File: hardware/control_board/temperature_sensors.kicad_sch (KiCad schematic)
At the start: 24 parts, among them J5 PT100, J5 TC, U2 MAX6675, U5 MCP6N11-005, U7 MCP6001

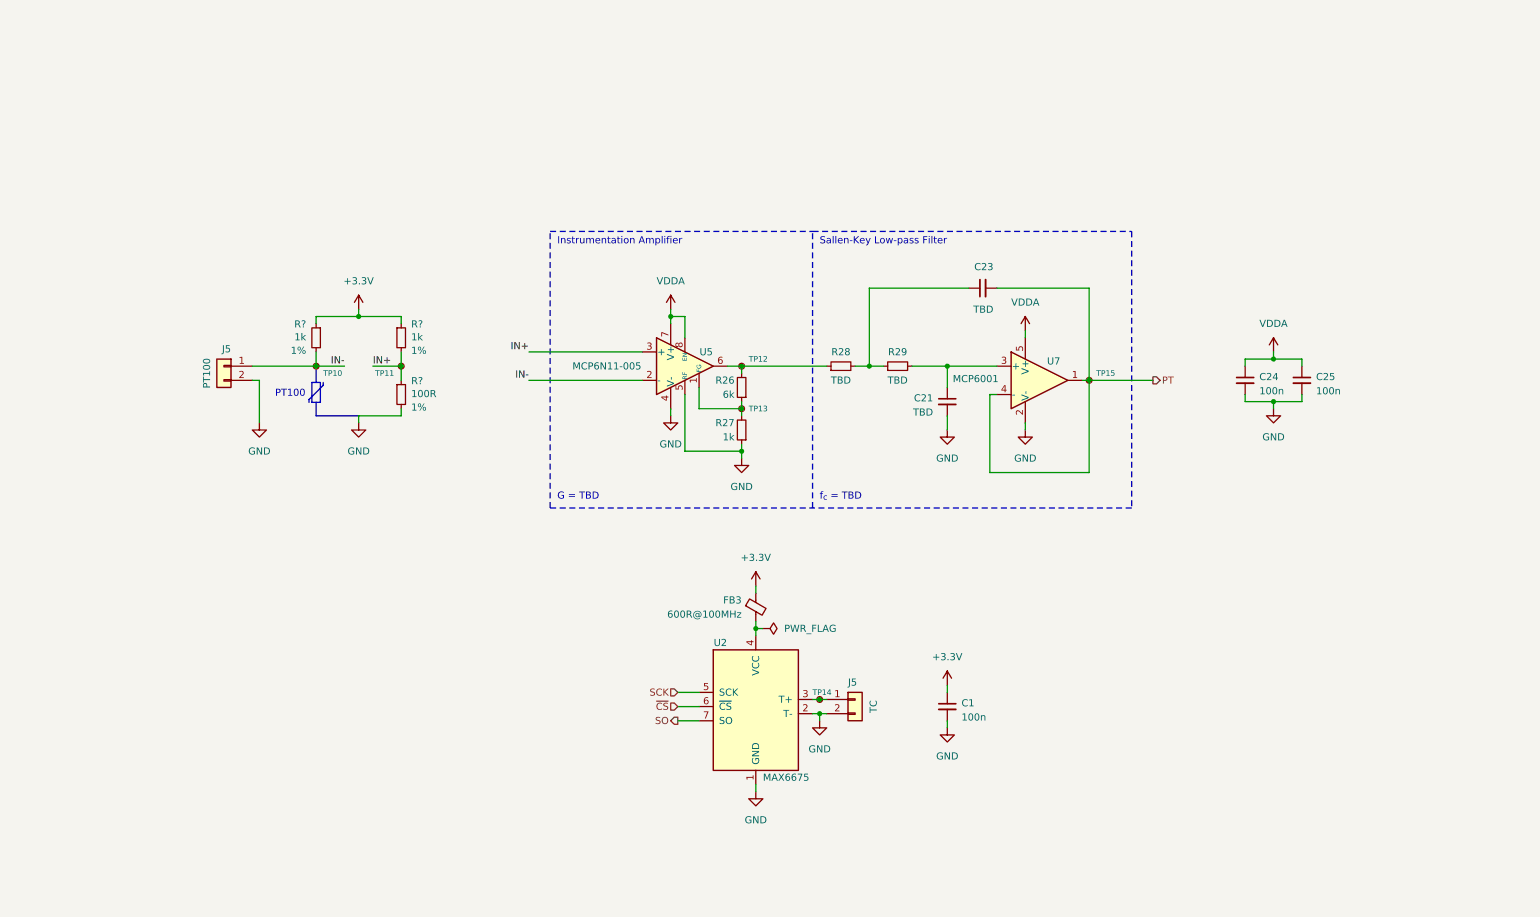
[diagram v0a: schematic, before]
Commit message: Adjust component values
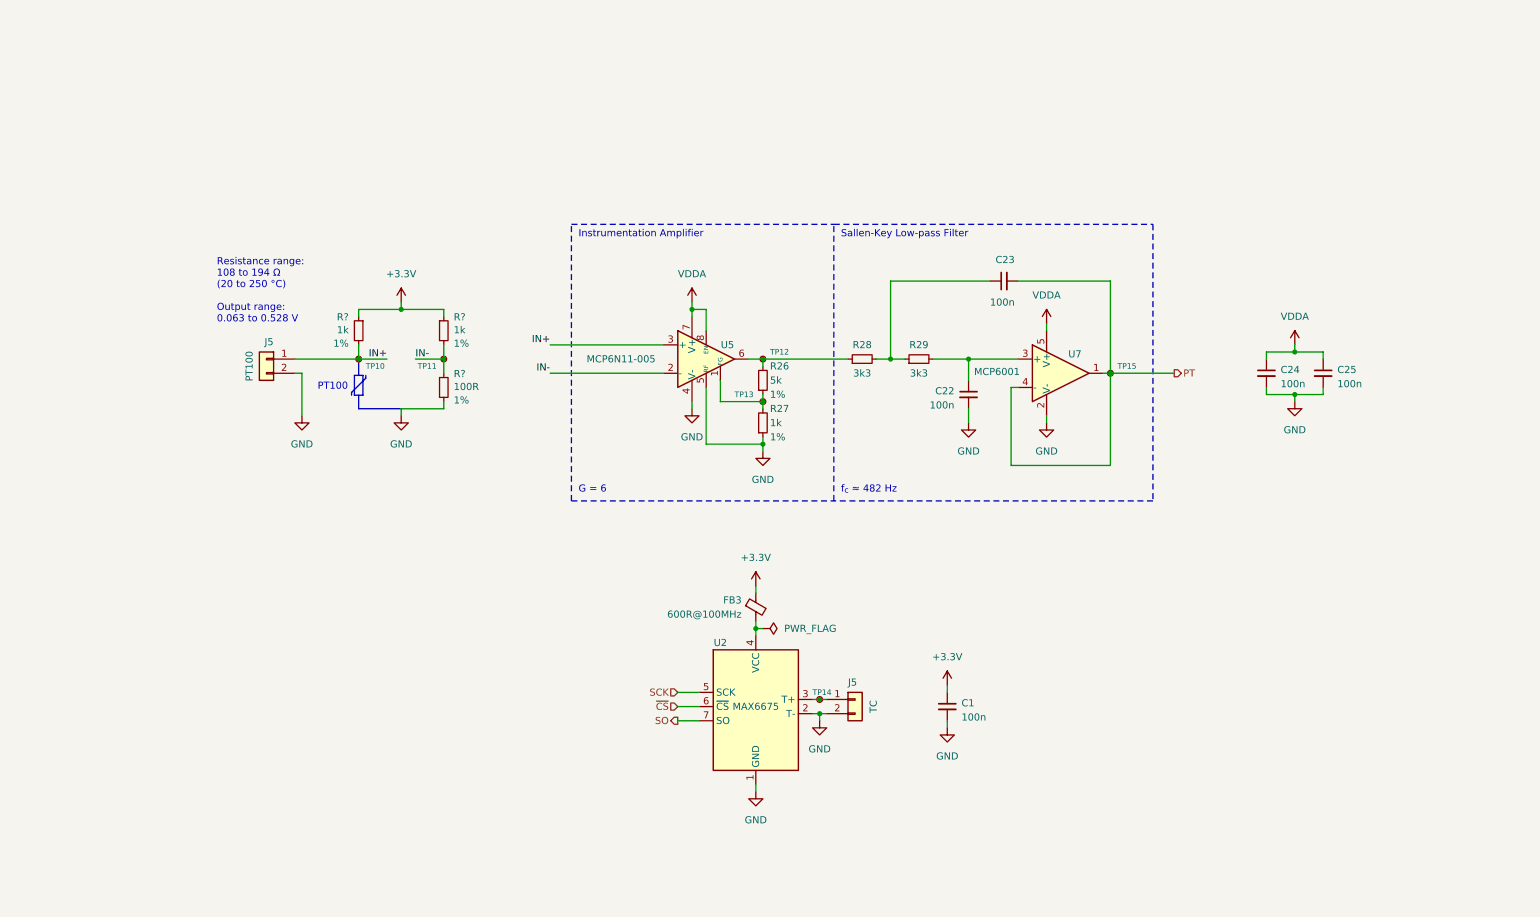
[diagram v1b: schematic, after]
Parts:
- C22: renamed from C21; value TBD -> 100n
- C23: value TBD -> 100n
- FB3: footprint (none) -> Inductor_SMD:L_0603_1608Metric
- R26: value 6k -> 5k; Tolerance (none) -> 1%
- R27: Tolerance (none) -> 1%
- R28, R29: value TBD -> 3k3
- U5: value MCP6N11-005 -> MCP6N11-005
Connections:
- net IN+: now also J5.1 (Pin_1), R?.2, TP10.1; no longer R?.1, R?.2, TP11.1
- net IN-: now also R?.1, R?.2, TP11.1; no longer J5.1 (Pin_1), R?.2, TP10.1
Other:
- note added: "G = 6"
- note added: "Resistance range: 108 to 194 Ω (20 to 250 °C) Output range: 0.063 to 0.528 V"
- note added: "f_{c} ≈ 482 Hz"
- note removed: "G = TBD"
- note removed: "f_{c} = TBD"
- moved on the sheet: C22, C23, C24, C25, J5, R26, R27, R28, R29, R?, TP10, TP11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

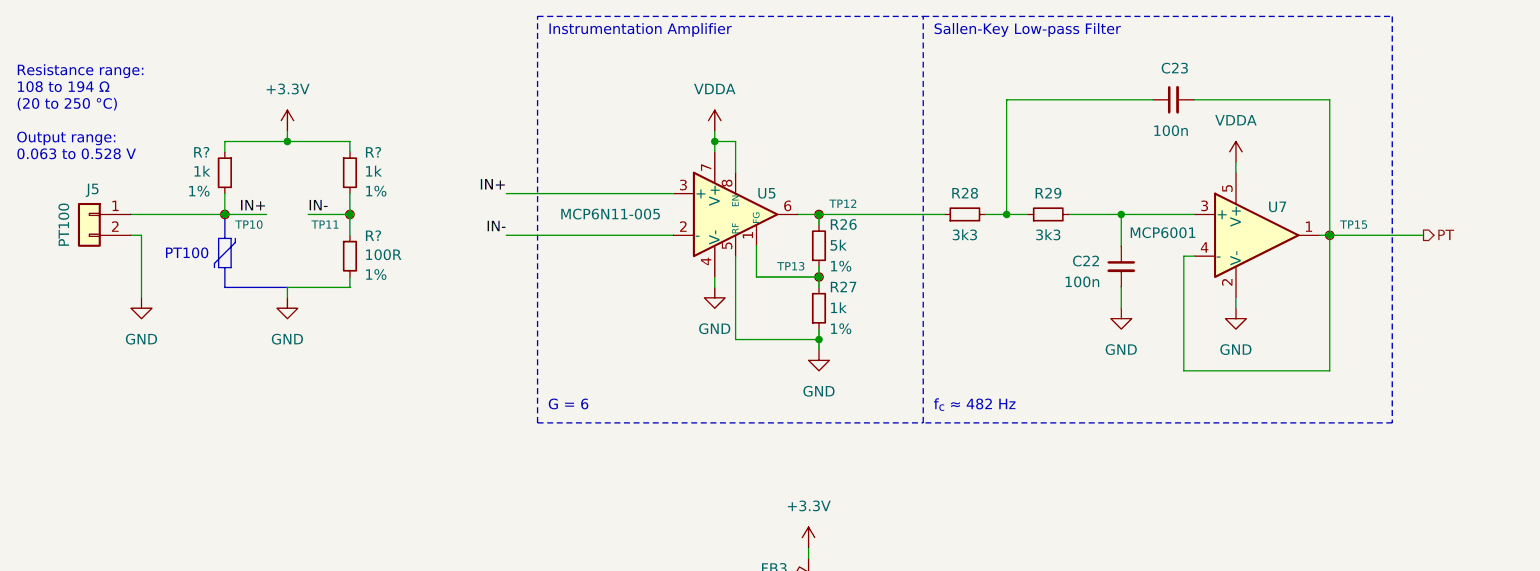
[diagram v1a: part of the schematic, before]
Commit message: Use a 3-wire RTD configuration
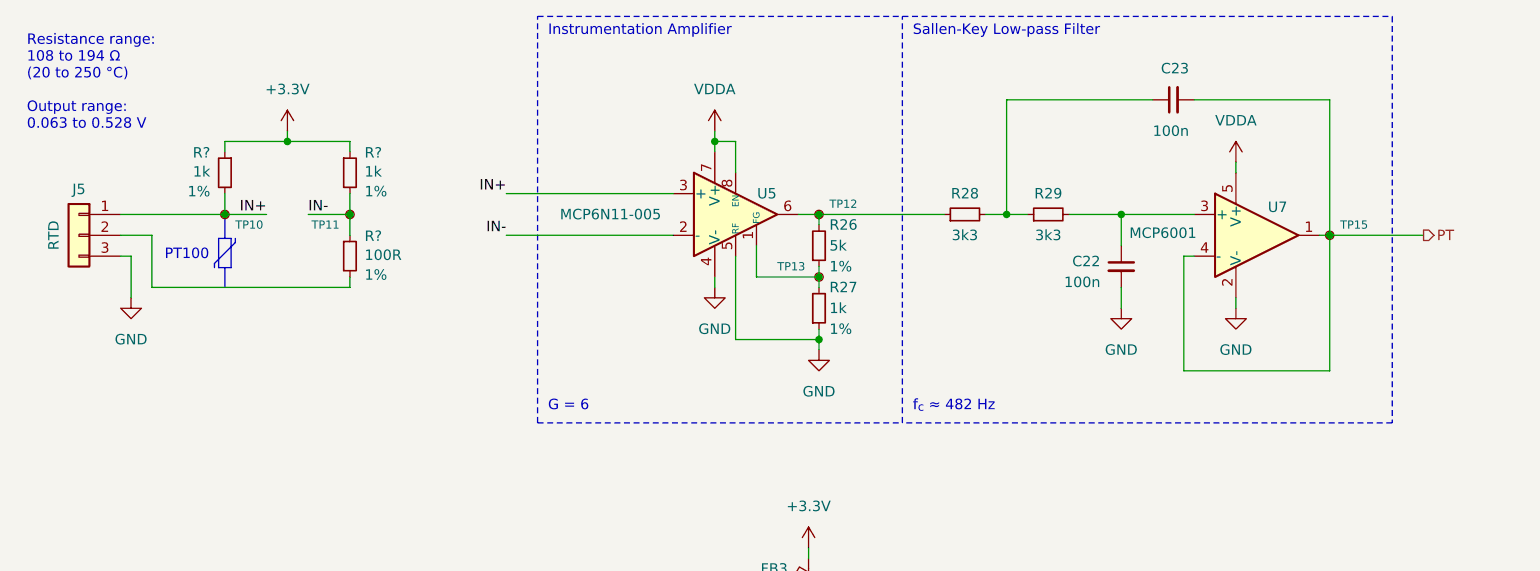
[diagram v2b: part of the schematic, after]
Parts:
- J5: value PT100 -> RTD; footprint Connector_JST:JST_XH_B2B-XH-AM_1x02_P2.50mm_Vertical -> Connector_JST:JST_XH_B3B-XH-A_1x03_P2.50mm_Vertical; symbol Connector_Generic:Conn_01x02 -> Connector_Generic:Conn_01x03
- J5: footprint Connector_JST:JST_XH_B2B-XH-AM_1x02_P2.50mm_Vertical -> Connector_JST:JST_XH_B2B-XH-A_1x02_P2.50mm_Vertical
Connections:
- net GND: now also J5.3 (Pin_3); no longer J5.2 (Pin_2), R?.2
- new net: J5.2 (Pin_2), R?.2
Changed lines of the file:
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@@
+    (stroke (width 0) (type default))
+  )
+  (wire (pts (xy 63.5 81.28) (xy 62.23 81.28))
     (stroke (width 0) (type default))
   )
@@
     (stroke (width 0) (type default))
   )
+  (wire (pts (xy 66.04 78.74) (xy 66.04 85.09))
+    (stroke (width 0) (type default))
+  )
   (wire (pts (xy 247.65 76.2) (xy 247.65 74.93))
     (stroke (width 0) (type default))
@@
     (stroke (width 0) (type default))
   )
-  (wire (pts (xy 64.77 78.74) (xy 63.5 78.74))
-    (stroke (width 0) (type default))
-  )
-  (polyline (pts (xy 160.02 101.6) (xy 160.02 52.07))
+  (polyline (pts (xy 157.48 101.6) (xy 157.48 52.07))
     (stroke (width 0) (type dash))
   )
@@
     (stroke (width 0) (type default))
   )
-  (wire (pts (xy 64.77 86.36) (xy 64.77 78.74))
+  (wire (pts (xy 63.5 81.28) (xy 63.5 86.36))
     (stroke (width 0) (type default))
   )
@@
     (stroke (width 0) (type default))
   )
+  (wire (pts (xy 62.23 78.74) (xy 66.04 78.74))
+    (stroke (width 0) (type default))
+  )
   (wire (pts (xy 90.17 76.2) (xy 85.09 76.2))
     (stroke (width 0) (type default))
@@
     (stroke (width 0) (type default))
   )
-  (wire (pts (xy 82.55 85.09) (xy 82.55 86.36))
-    (stroke (width 0) (type default))
-  )
   (wire (pts (xy 198.12 87.63) (xy 198.12 86.36))
     (stroke (width 0) (type default))
@@
     (stroke (width 0) (type default))
   )
-  (polyline (pts (xy 160.02 52.07) (xy 217.17 52.07))
+  (polyline (pts (xy 157.48 52.07) (xy 217.17 52.07))
     (stroke (width 0) (type dash))
   )
@@
     (stroke (width 0) (type default))
   )
-  (polyline (pts (xy 82.55 85.09) (xy 74.93 85.09))
-    (stroke (width 0) (type default))
-  )
   (wire (pts (xy 134.62 85.09) (xy 134.62 83.82))
     (stroke (width 0) (type default))
@@
     (stroke (width 0) (type default))
   )
-  (polyline (pts (xy 217.17 101.6) (xy 160.02 101.6))
+  (polyline (pts (xy 217.17 101.6) (xy 157.48 101.6))
     (stroke (width 0) (type dash))
   )
-  (polyline (pts (xy 113.03 101.6) (xy 160.02 101.6))
+  (polyline (pts (xy 113.03 101.6) (xy 157.48 101.6))
     (stroke (width 0) (type dash))
   )
@@
   )
   (wire (pts (xy 157.48 137.16) (xy 158.75 137.16))
+    (stroke (width 0) (type default))
+  )
+  (wire (pts (xy 66.04 85.09) (xy 90.17 85.09))
     (stroke (width 0) (type default))
   )
@@
     (stroke (width 0) (type default))
   )
-  (wire (pts (xy 82.55 85.09) (xy 90.17 85.09))
-    (stroke (width 0) (type default))
-  )
   (wire (pts (xy 147.32 124.46) (xy 146.05 124.46))
     (stroke (width 0) (type default))
@@
     (stroke (width 0) (type default))
   )
-  (wire (pts (xy 63.5 76.2) (xy 74.93 76.2))
+  (wire (pts (xy 62.23 76.2) (xy 74.93 76.2))
     (stroke (width 0) (type default))
   )
@@
     (stroke (width 0) (type default))
   )
-  (polyline (pts (xy 113.03 52.07) (xy 160.02 52.07))
+  (polyline (pts (xy 113.03 52.07) (xy 157.48 52.07))
     (stroke (width 0) (type dash))
   )
@@
   )
   (text "Resistance range:\n108 to 194 Ω\n(20 to 250 °C)\n\nOutput range:\n0.063 to 0.528 V"
-    (at 49.53 69.85 0)
+    (at 50.8 66.04 0)
     (effects (font (size 1.27 1.27)) (justify left bottom))
   )
@@
     (effects (font (size 1.27 1.27)) (justify left bottom))
   )
-  (text "Sallen-Key Low-pass Filter" (at 161.29 54.61 0)
+  (text "Sallen-Key Low-pass Filter" (at 158.75 54.61 0)
     (effects (font (size 1.27 1.27)) (justify left bottom))
   )
-  (text "f_{c} ≈ 482 Hz" (at 161.29 100.33 0)
+  (text "f_{c} ≈ 482 Hz" (at 158.75 100.33 0)
     (effects (font (size 1.27 1.27)) (justify left bottom))
   )
@@
         (path "/b652b05a-4e3d-4ad1-b032-18886abe7d45/02711725-e382-48ba-bf33-23fe46c66e66"
           (reference "#PWR070") (unit 1)
-        )
-      )
-    )
-  )
-  (symbol (lib_id "power:GND") (at 82.55 86.36 0) (unit 1)
-    (in_bom yes) (on_board yes) (dnp no)
-    (property "Reference" "#PWR?" (at 82.55 92.71 0)
-      (effects (font (size 1.27 1.27)) hide)
-    )
-    (property "Value" "GND" (at 82.55 91.44 0)
-      (effects (font (size 1.27 1.27)))
-    )
-    (property "Footprint" "" (at 82.55 86.36 0)
-      (effects (font (size 1.27 1.27)) hide)
-    )
-    (property "Datasheet" "" (at 82.55 86.36 0)
-      (effects (font (size 1.27 1.27)) hide)
-    )
-    (pin "1")
-    (instances
-      (project "Traction_Control_System"
-        (path "/9e519d0e-7843-4728-8a6d-7ea5f5f4d223/00000000-0000-0000-0000-00006194bc41"
-          (reference "#PWR?") (unit 1)
-        )
-        (path "/9e519d0e-7843-4728-8a6d-7ea5f5f4d223/00000000-0000-0000-0000-000061c1de38/00000000-0000-0000-0000-000061c3ba92"
-          (reference "#PWR?") (unit 1)
-        )
-        (path "/9e519d0e-7843-4728-8a6d-7ea5f5f4d223/00000000-0000-0000-0000-000061c1de38/00000000-0000-0000-0000-000061b1e697"
-          (reference "#PWR?") (unit 1)
-        )
-        (path "/9e519d0e-7843-4728-8a6d-7ea5f5f4d223/00000000-0000-0000-0000-000061c1de38/00000000-0000-0000-0000-000061c3ba8e"
-          (reference "#PWR?") (unit 1)
-        )
-        (path "/9e519d0e-7843-4728-8a6d-7ea5f5f4d223/00000000-0000-0000-0000-000061acb470"
-          (reference "#PWR?") (unit 1)
-        )
-        (path "/9e519d0e-7843-4728-8a6d-7ea5f5f4d223/00000000-0000-0000-0000-000061c1de38/00000000-0000-0000-0000-000061b1e693"
-          (reference "#PWR?") (unit 1)
-        )
-      )
-      (project "control_board"
-        (path "/b652b05a-4e3d-4ad1-b032-18886abe7d45/02711725-e382-48ba-bf33-23fe46c66e66"
-          (reference "#PWR067") (unit 1)
         )
       )
@@
     )
   )
-  (symbol (lib_id "Connector_Generic:Conn_01x02") (at 58.42 76.2 0) (mirror y) (unit 1)
-    (in_bom yes) (on_board yes) (dnp no)
-    (property "Reference" "J5" (at 59.69 72.39 0)
-      (effects (font (size 1.27 1.27)) (justify left top))
-    )
-    (property "Value" "PT100" (at 54.61 77.47 90)
+  (symbol (lib_id "Connector_Generic:Conn_01x03") (at 57.15 78.74 0) (mirror y) (unit 1)
+    (in_bom yes) (on_board yes) (dnp no)
+    (property "Reference" "J5" (at 57.15 72.39 0)
+      (effects (font (size 1.27 1.27)) (justify top))
+    )
+    (property "Value" "RTD" (at 53.34 78.74 90)
       (effects (font (size 1.27 1.27)) (justify bottom))
     )
-    (property "Footprint" "Connector_JST:JST_XH_B2B-XH-AM_1x02_P2.50mm_Vertical" (at 58.42 76.2 0)
-      (effects (font (size 1.27 1.27)) hide)
-    )
-    (property "Datasheet" "~" (at 58.42 76.2 0)
-      (effects (font (size 1.27 1.27)) hide)
-    )
-    (pin "1")
-    (pin "2")
+    (property "Footprint" "Connector_JST:JST_XH_B3B-XH-A_1x03_P2.50mm_Vertical" (at 57.15 78.74 0)
+      (effects (font (size 1.27 1.27)) hide)
+    )
+    (property "Datasheet" "~" (at 57.15 78.74 0)
+      (effects (font (size 1.27 1.27)) hide)
+    )
+    (pin "1")
+    (pin "2")
+    (pin "3")
     (instances
       (project "control_board"
@@
     )
   )
-  (symbol (lib_id "power:GND") (at 64.77 86.36 0) (unit 1)
-    (in_bom yes) (on_board yes) (dnp no)
-    (property "Reference" "#PWR?" (at 64.77 92.71 0)
-      (effects (font (size 1.27 1.27)) hide)
-    )
-    (property "Value" "GND" (at 64.77 91.44 0)
-      (effects (font (size 1.27 1.27)))
-    )
-    (property "Footprint" "" (at 64.77 86.36 0)
-      (effects (font (size 1.27 1.27)) hide)
-    )
-    (property "Datasheet" "" (at 64.77 86.36 0)
+  (symbol (lib_id "power:GND") (at 63.5 86.36 0) (unit 1)
+    (in_bom yes) (on_board yes) (dnp no)
+    (property "Reference" "#PWR?" (at 63.5 92.71 0)
+      (effects (font (size 1.27 1.27)) hide)
+    )
+    (property "Value" "GND" (at 63.5 91.44 0)
+      (effects (font (size 1.27 1.27)))
+    )
+    (property "Footprint" "" (at 63.5 86.36 0)
+      (effects (font (size 1.27 1.27)) hide)
+    )
+    (property "Datasheet" "" (at 63.5 86.36 0)
       (effects (font (size 1.27 1.27)) hide)
     )
@@
       (effects (font (size 1.27 1.27)) (justify top))
     )
-    (property "Footprint" "Connector_JST:JST_XH_B2B-XH-AM_1x02_P2.50mm_Vertical" (at 163.83 137.16 0)
-      (effects (font (size 1.27 1.27)) hide)
-    )
+    (property "Footprint" "Connector_JST:JST_XH_B2B-XH-A_1x02_P2.50mm_Vertical" (at 163.83 137.16 0)
+      (effects (font (size 1.27 1.27)) hide)
+    )

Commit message: Assign footprints to components
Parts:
- J5: Component (none) -> B3B-XH-A (LF)(SN)
- J5: Component (none) -> B2B-XH-A (LF)(SN)
- U5: value MCP6N11-005 -> MCP6N11T-005E; footprint Package_DFN_QFN:TDFN-8-1EP_3x2mm_P0.5mm_EP1.80x1.65mm -> Package_SO:SOIC-8_3.9x4.9mm_P1.27mm
- U7: value MCP6001 -> MCP6001T
- renumbered TP10 to TP12, TP11 to TP13, TP12 to TP14, TP13 to TP15, TP14 to TP16, TP15 to TP17
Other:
- note added: "RTD"
- note added: "TC"
- moved on the sheet: C1, C22, C23, C24, C25, FB3, J5, R26, R27, R28, R29, R?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
